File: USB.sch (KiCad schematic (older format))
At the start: 41 parts, among them J6 USB_A, J7 USB_B, U10 USB3320, U11 MIC2025-1YMM, U12 USB3320, U20 xc7z020clg484, Y1 24.000MHZ, Y2 24.000MHZ

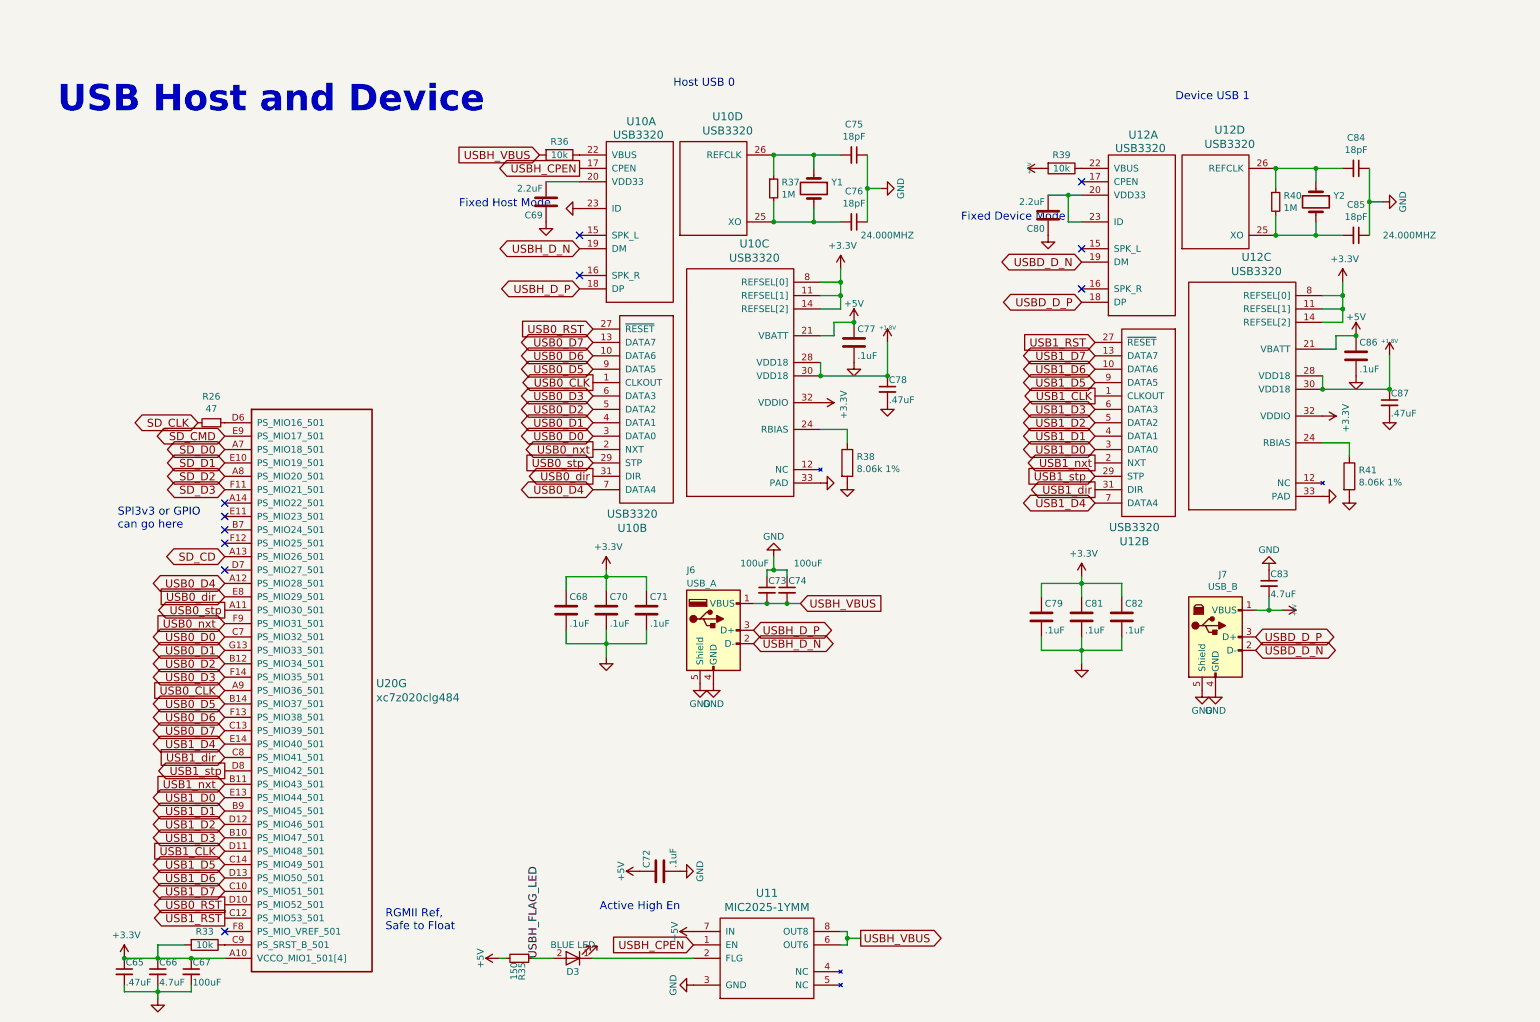
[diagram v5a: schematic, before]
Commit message: finished review with gerber output. still need to relocate rangefinders / LEDs
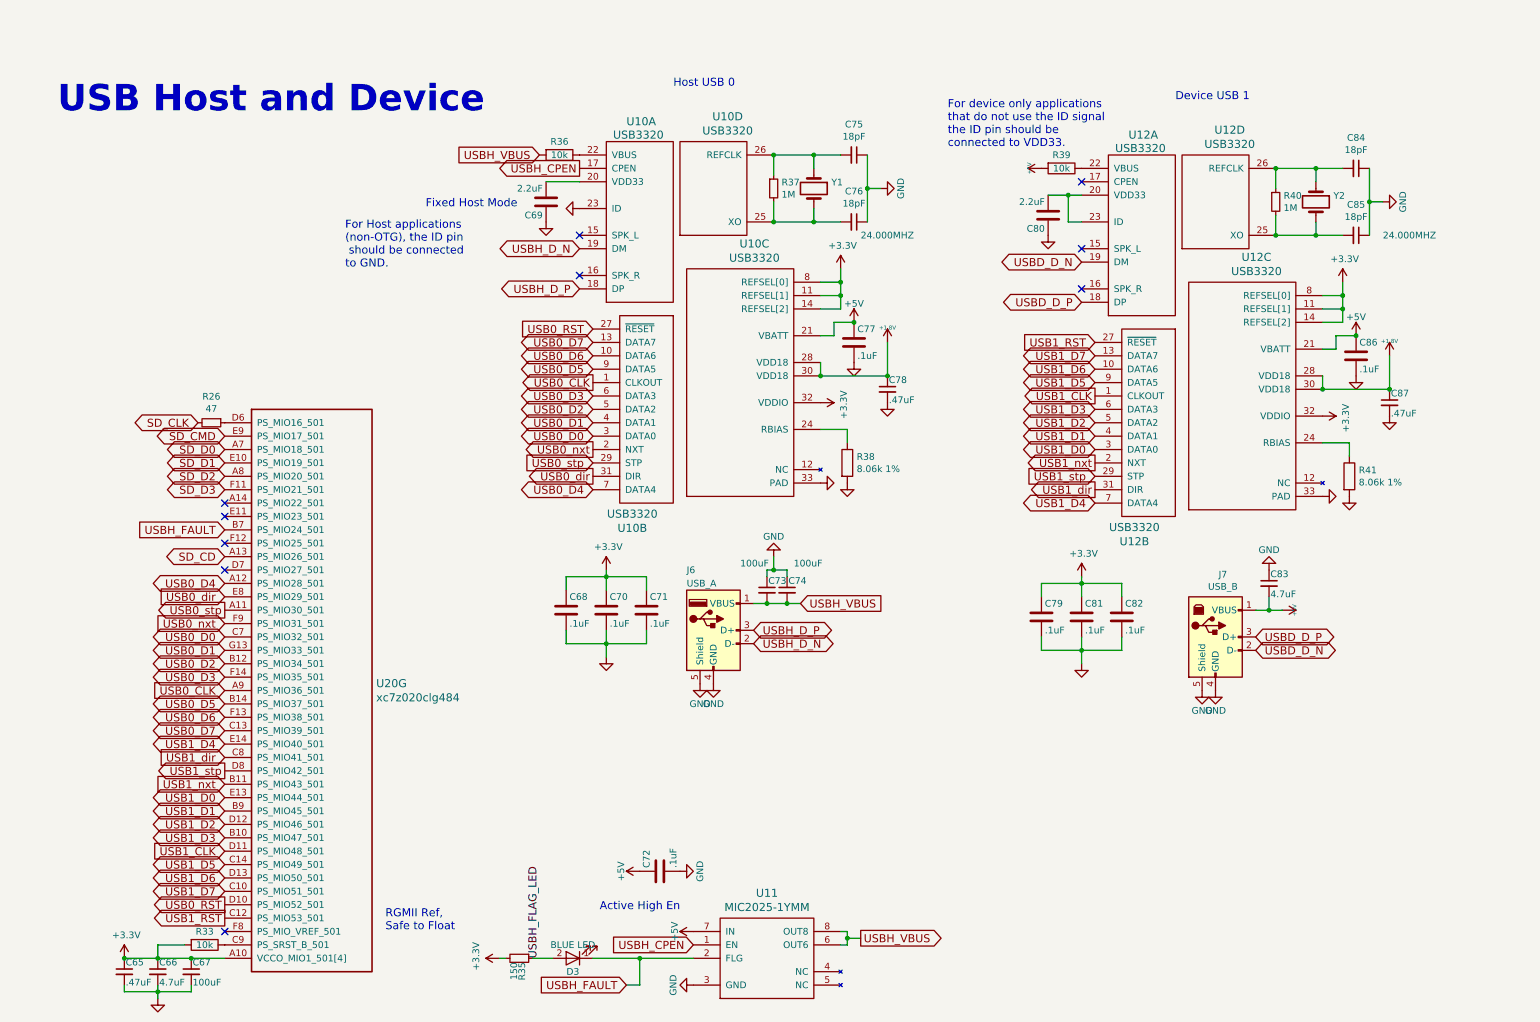
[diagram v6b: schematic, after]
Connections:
- net +3V3: now also R35.2
- net +5V: no longer R35.2
- net USBH_FAULT: now reaches D3.1 (K), U11.2 (FLG)
- net USBH_FAULT: now also U20.B7 (PS_MIO24_501)
- no-connect marks 11 -> 10
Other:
- note added: "For Host applications \n(non-OTG), the ID pin\n should be connected \nto GND."
- note added: "For device only applications\nthat do not use the ID signal\nthe ID pin should be \nconnected to VDD33."
- note removed: "Fixed Device Mode"
- note removed: "SPI3v3 or GPIO \ncan go here\n"

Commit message: some part changes for BOM clarification
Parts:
- C65, C78, C87: MFR Murata -> Yageo; MPN GRM188R71C474KA88D -> CC0402KRX5R5BB474; SPN 490-3295-1-ND -> 311-1684-1-ND
- C66, C83: MPN GRM21BR61A475KA73L -> GRM155R60G475ME47D; SPN 490-9750-1-ND -> 490-11980-1-ND
- C68, C70, C71, C72, C77, C79, C81, C82, C86: MFR Murata -> Yageo; MPN GRM188R71C104KA01D -> CC0402KRX7R6BB104; SPN 490-1532-1-ND -> 311-1345-1-ND
